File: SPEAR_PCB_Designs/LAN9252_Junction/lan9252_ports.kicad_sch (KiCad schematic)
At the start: 36 parts, among them J1 SM04B-GHS-TB, J2 SM04B-GHS-TB, T1 H1102NLT, T2 H1102NLT, U1 24FC512

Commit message: Almost finished board
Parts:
- removed C1, C2: C, Capacitor_SMD:C_0201_0603Metric, symbol Device:C
- removed C3, C4: 1000 uF, Capacitor_SMD:C_0201_0603Metric, symbol Device:C
- removed J2: SM04B-GHS-TB, Connector_JST:JST_GH_SM04B-GHS-TB_1x04-1MP_P1.25mm_Horizontal, symbol Connector_Generic_MountingPin:Conn_01x04_MountingPin
- removed R1, R2, R3, R4, R5, R6: 49.9 R, Resistor_SMD:R_0603_1608Metric, symbol Device:R_US
- removed T1, T2: H1102NLT, Transformer_SMD:Transformer_Pulse_H1100NL, symbol H1102NLT:H1102NLT
- added C18, C19, C20, C21, C22, C23, C24, C25: 10p, Capacitor_SMD:C_0402_1005Metric, symbol Device:C
- added C26, C27: 22n, Capacitor_SMD:C_0402_1005Metric, symbol Device:C
- added C28, C29: 1000 pF, Capacitor_SMD:C_0402_1005Metric, symbol Device:C
- added J1: SM04B-GHS-TB, Connector_JST:JST_GH_SM04B-GHS-TB_1x04-1MP_P1.25mm_Horizontal, symbol LAN9252 Symbols:SM04B-GHS-TB
- added R10, R11, R12: 49.9R 1%, Resistor_SMD:R_0402_1005Metric, symbol Device:R_US
- added R17: 1k, Resistor_SMD:R_0402_1005Metric, symbol Device:R_US
- added R18, R19: 75R 1%, Resistor_SMD:R_0402_1005Metric, symbol Device:R_US
- added T1, T2: H1102NLT, SPEAR_FOOTPRINTS:XFMR_H1102NLT, symbol LAN9252 Symbols:H1102NLT
- C30: renamed from C5; footprint Capacitor_SMD:C_0201_0603Metric -> Capacitor_SMD:C_0402_1005Metric
- D1, D2, D3: footprint LED_SMD:LED_0201_0603Metric -> LED_SMD:LED_0603_1608Metric
- J2: renamed from J1; symbol Connector_Generic_MountingPin:Conn_01x04_MountingPin -> LAN9252 Symbols:SM04B-GHS-TB; now in the parts list
- R13: value 1k -> 49.9R 1%; footprint Resistor_SMD:R_0603_1608Metric -> Resistor_SMD:R_0402_1005Metric
- R14: value 75 -> 49.9R 1%; footprint Resistor_SMD:R_0603_1608Metric -> Resistor_SMD:R_0402_1005Metric
- R15: value 75 -> 0R; footprint Resistor_SMD:R_0603_1608Metric -> Resistor_SMD:R_0402_1005Metric
- R16: renamed from R10; value 49.9 R -> 0R; footprint Resistor_SMD:R_0603_1608Metric -> Resistor_SMD:R_0402_1005Metric
- R20: renamed from R11; value 75 -> 75R 1%; footprint Resistor_SMD:R_0603_1608Metric -> Resistor_SMD:R_0402_1005Metric
- R21: renamed from R12; value 75 -> 75R 1%; footprint Resistor_SMD:R_0603_1608Metric -> Resistor_SMD:R_0402_1005Metric
- R22: renamed from R16; footprint Resistor_SMD:R_0603_1608Metric -> Resistor_SMD:R_0402_1005Metric
- R23: renamed from R17; footprint Resistor_SMD:R_0603_1608Metric -> Resistor_SMD:R_0402_1005Metric
- R24: renamed from R18; footprint Resistor_SMD:R_0603_1608Metric -> Resistor_SMD:R_0402_1005Metric
- R25: renamed from R19; footprint Resistor_SMD:R_0603_1608Metric -> Resistor_SMD:R_0402_1005Metric
- R26: renamed from R20; footprint Resistor_SMD:R_0603_1608Metric -> Resistor_SMD:R_0402_1005Metric
- R27: renamed from R21; footprint Resistor_SMD:R_0603_1608Metric -> Resistor_SMD:R_0402_1005Metric
- R28: renamed from R22; footprint Resistor_SMD:R_0603_1608Metric -> Resistor_SMD:R_0402_1005Metric
- R29: renamed from R23; footprint Resistor_SMD:R_0603_1608Metric -> Resistor_SMD:R_0402_1005Metric
- R7, R8, R9: value 49.9 R -> 49.9R 1%; footprint Resistor_SMD:R_0603_1608Metric -> Resistor_SMD:R_0402_1005Metric
- renumbered U1 to U2
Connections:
- net GNDREF is gone; now on net GND: C30.2, R23.1, U2.4 (VSS)
- net GND: now also D1.1 (K), C18.2, C19.2, C20.2, C21.2, C22.2, C23.2, C24.2, C25.2, C26.2, C27.2, C28.2, C29.2; no longer D1.2 (A)
- net GPIO1: now also R17.1; no longer R13.1
- net RXA N: now also R13.2, C24.1, T2.3; no longer R7.2
- net RXA P: now also C22.1, R11.2, T2.1
- net RXB N: now also R14.2, C25.1, T1.6; no longer R8.2
- net RXB P: now also C23.1, R12.2, T1.8
- net TXA N: now also R9.2, C20.1, T2.8
- net TXA P: now also R7.2, C18.1, T2.6
- net TXB N: now also C21.1, R10.2, T1.1
- net TXB P: now also R8.2, C19.1, T1.3
- net VDD33TXRX1: now also R13.1, R15.1, R11.1
- net VDD33TXRX2: now also R14.1, R10.1, R12.1
- net at R15.2: now also C26.1, T2.2, T2.7; no longer R14.2
- net at R21.1: now also T2.10
- net at R20.2, R21.2: now also C29.1
- net at R16.2: now also C27.1, T1.2, T1.7
- net TXA+: now reaches J2.1 (Pin_1)
- net TXA+: now also T2.9
- net TXA-: now reaches J2.2 (Pin_2)
- net TXA-: now also T2.11
- net RXA+: now reaches J2.3 (Pin_3)
- net RXA+: now also T2.14
- net RXA-: now reaches J2.4 (Pin_4)
- net RXA-: now also T2.16
- net at R20.1: now also T2.15
- new net: D1.2 (A), R17.2
- new net: R19.1, T1.10
- new net: R18.1, T1.15
- new net: C28.1, R18.2, R19.2
- new net RXB+: J1.3 (Pin_3), T1.14
- new net RXB-: J1.4 (Pin_4), T1.16
- new net TXB+: J1.1 (Pin_1), T1.9
- new net TXB-: J1.2 (Pin_2), T1.11
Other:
- note added: "Polarity, and transmit and receive were swapped for routing purposes. Auto-MDIX and polarity detection will correct for this."
- moved on the sheet: D1, D3, J2, R16, R20, R21, R22, R24, R25, R26, R27

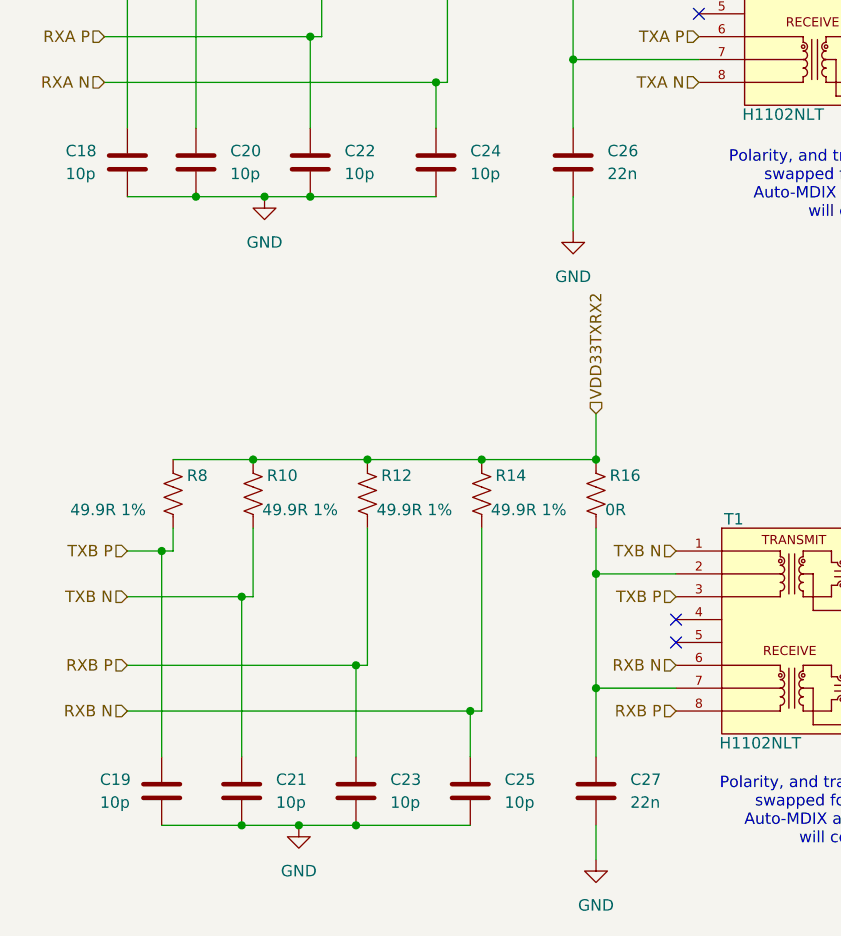
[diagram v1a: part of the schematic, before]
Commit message: Added Fabrication Spec
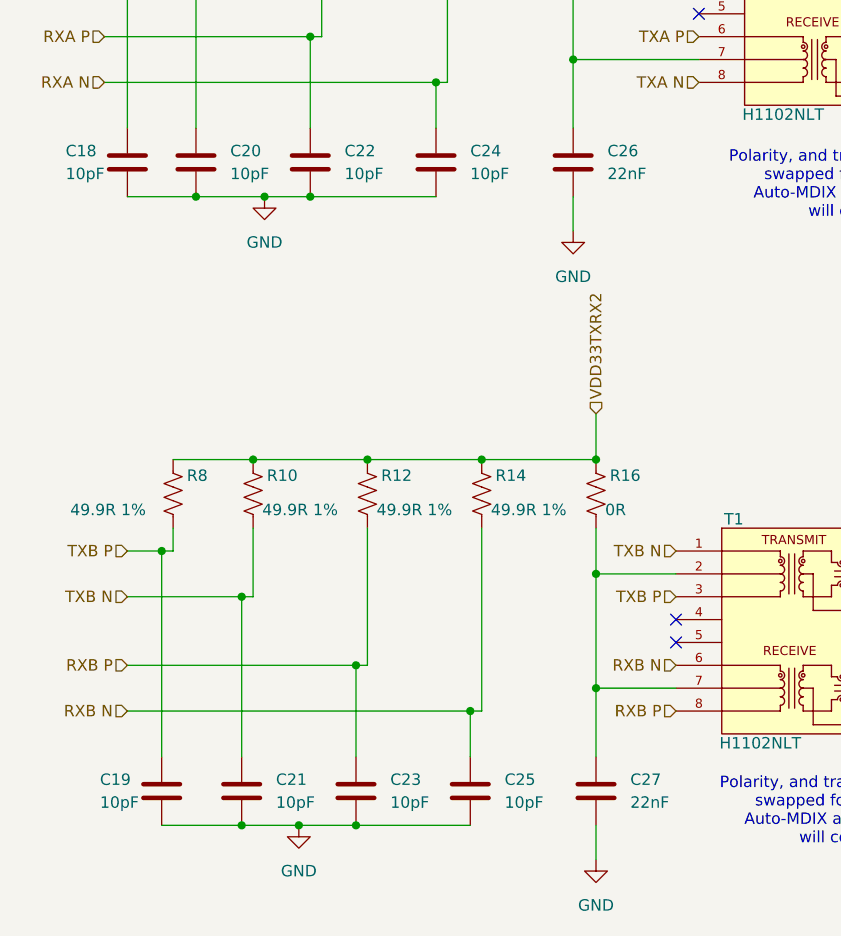
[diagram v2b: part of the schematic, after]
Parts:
- C18, C19, C20, C21, C22, C23, C24, C25: value 10p -> 10pF; DigiKey_Part_Number (none) -> 1276-1139-1-ND
- C26, C27: value 22n -> 22nF; DigiKey_Part_Number (none) -> 399-C0402C223K5RACTUCT-ND
- C28, C29: DigiKey_Part_Number (none) -> 399-C0402C102K5RACTUCT-ND
- C30: DigiKey_Part_Number (none) -> 445-5932-1-ND
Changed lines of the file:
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@@
+			)
+		)
+		(property "DigiKey_Part_Number" "445-5932-1-ND"
+			(at 200.66 125.73 0)
+			(effects
+				(font
+					(size 1.27 1.27)
+				)
+				(hide yes)
 			)
 		)
@@
 		)
 		(property "STANDARD" ""
+			(at 137.16 142.24 0)
+			(effects
+				(font
+					(size 1.27 1.27)
+				)
+				(hide yes)
+			)
+		)
+		(property "DigiKey_Part_Number" "399-C0402C102K5RACTUCT-ND"
 			(at 137.16 142.24 0)
 			(effects
@@
 			)
 		)
-		(property "Value" "10p"
+		(property "Value" "10pF"
 			(at 64.77 77.4699 0)
 			(effects
@@
 		)
 		(property "STANDARD" ""
+			(at 60.96 76.2 0)
+			(effects
+				(font
+					(size 1.27 1.27)
+				)
+				(hide yes)
+			)
+		)
+		(property "DigiKey_Part_Number" "1276-1139-1-ND"
 			(at 60.96 76.2 0)
 			(effects
@@
 			)
 		)
-		(property "Value" "22n"
+		(property "Value" "22nF"
 			(at 82.55 147.3199 0)
 			(effects
@@
 		)
 		(property "STANDARD" ""
+			(at 78.74 146.05 0)
+			(effects
+				(font
+					(size 1.27 1.27)
+				)
+				(hide yes)
+			)
+		)
+		(property "DigiKey_Part_Number" "399-C0402C223K5RACTUCT-ND"
 			(at 78.74 146.05 0)
 			(effects
@@
 			)
 		)
-		(property "Value" "10p"
+		(property "Value" "10pF"
 			(at 43.18 147.3199 0)
 			(effects
@@
 			)
 		)
+		(property "DigiKey_Part_Number" "1276-1139-1-ND"
+			(at 39.37 146.05 0)
+			(effects
+				(font
+					(size 1.27 1.27)
+				)
+				(hide yes)
+			)
+		)
 		(pin "2"
 		)
@@
 			)
 		)
-		(property "Value" "10p"
+		(property "Value" "10pF"
 			(at 23.622 147.32 0)
 			(effects
@@
 		)
 		(property "STANDARD" ""
+			(at 30.48 146.05 0)
+			(effects
+				(font
+					(size 1.27 1.27)
+				)
+				(hide yes)
+			)
+		)
+		(property "DigiKey_Part_Number" "1276-1139-1-ND"
 			(at 30.48 146.05 0)
 			(effects
@@
 			)
 		)
-		(property "Value" "10p"
+		(property "Value" "10pF"
 			(at 68.58 147.3199 0)
 			(effects
@@
 		)
 		(property "STANDARD" ""
+			(at 64.77 146.05 0)
+			(effects
+				(font
+					(size 1.27 1.27)
+				)
+				(hide yes)
+			)
+		)
+		(property "DigiKey_Part_Number" "1276-1139-1-ND"
 			(at 64.77 146.05 0)
 			(effects
@@
 			)
 		)
-		(property "Value" "10p"
+		(property "Value" "10pF"
 			(at 55.88 147.3199 0)
 			(effects
@@
 		)
 		(property "STANDARD" ""
+			(at 52.07 146.05 0)
+			(effects
+				(font
+					(size 1.27 1.27)
+				)
+				(hide yes)
+			)
+		)
+		(property "DigiKey_Part_Number" "1276-1139-1-ND"
 			(at 52.07 146.05 0)
 			(effects
@@
 			)
 		)
-		(property "Value" "10p"
+		(property "Value" "10pF"
 			(at 38.1 77.4699 0)
 			(effects
@@
 		)
 		(property "STANDARD" ""
+			(at 34.29 76.2 0)
+			(effects
+				(font
+					(size 1.27 1.27)
+				)
+				(hide yes)
+			)
+		)
+		(property "DigiKey_Part_Number" "1276-1139-1-ND"
 			(at 34.29 76.2 0)
 			(effects
@@
 			)
 		)
-		(property "Value" "10p"
+		(property "Value" "10pF"
 			(at 50.8 77.4699 0)
 			(effects
@@
 			)
 		)
+		(property "DigiKey_Part_Number" "1276-1139-1-ND"
+			(at 46.99 76.2 0)
+			(effects
+				(font
+					(size 1.27 1.27)
+				)
+				(hide yes)
+			)
+		)
 		(pin "2"
 		)
@@
 			)
 		)
-		(property "Value" "22n"
+		(property "Value" "22nF"
 			(at 80.01 77.4699 0)
 			(effects
@@
 			)
 		)
+		(property "DigiKey_Part_Number" "399-C0402C223K5RACTUCT-ND"
+			(at 76.2 76.2 0)
+			(effects
+				(font
+					(size 1.27 1.27)
+				)
+				(hide yes)
+			)
+		)
 		(pin "2"
 		)
@@
 			)
 		)
-		(property "Value" "10p"
+		(property "Value" "10pF"
 			(at 19.812 77.47 0)
 			(effects
@@
 			)
 		)
+		(property "DigiKey_Part_Number" "1276-1139-1-ND"
+			(at 26.67 76.2 0)
+			(effects
+				(font
+					(size 1.27 1.27)
+				)
+				(hide yes)
+			)
+		)
 		(pin "2"
 		)
@@
 			(at 147.32 72.39 0)
 			(effects
+				(font
+					(size 1.27 1.27)
+				)
+				(hide yes)
+			)
+		)
+		(property "DigiKey_Part_Number" "399-C0402C102K5RACTUCT-ND"
+			(at 147.32 72.39 0)
+			(effects

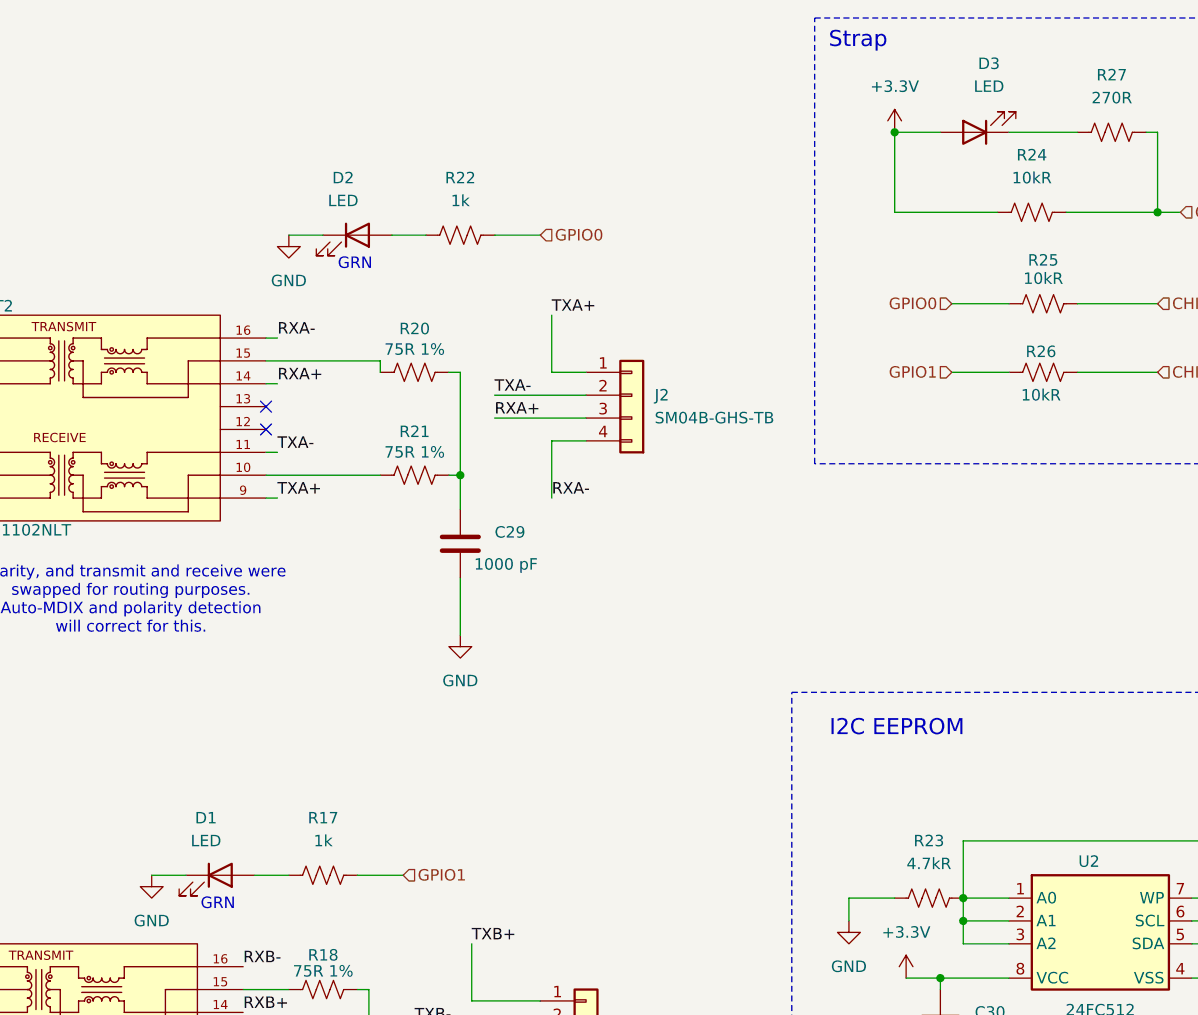
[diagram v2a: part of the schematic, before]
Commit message: Added BOM for the Junction Board
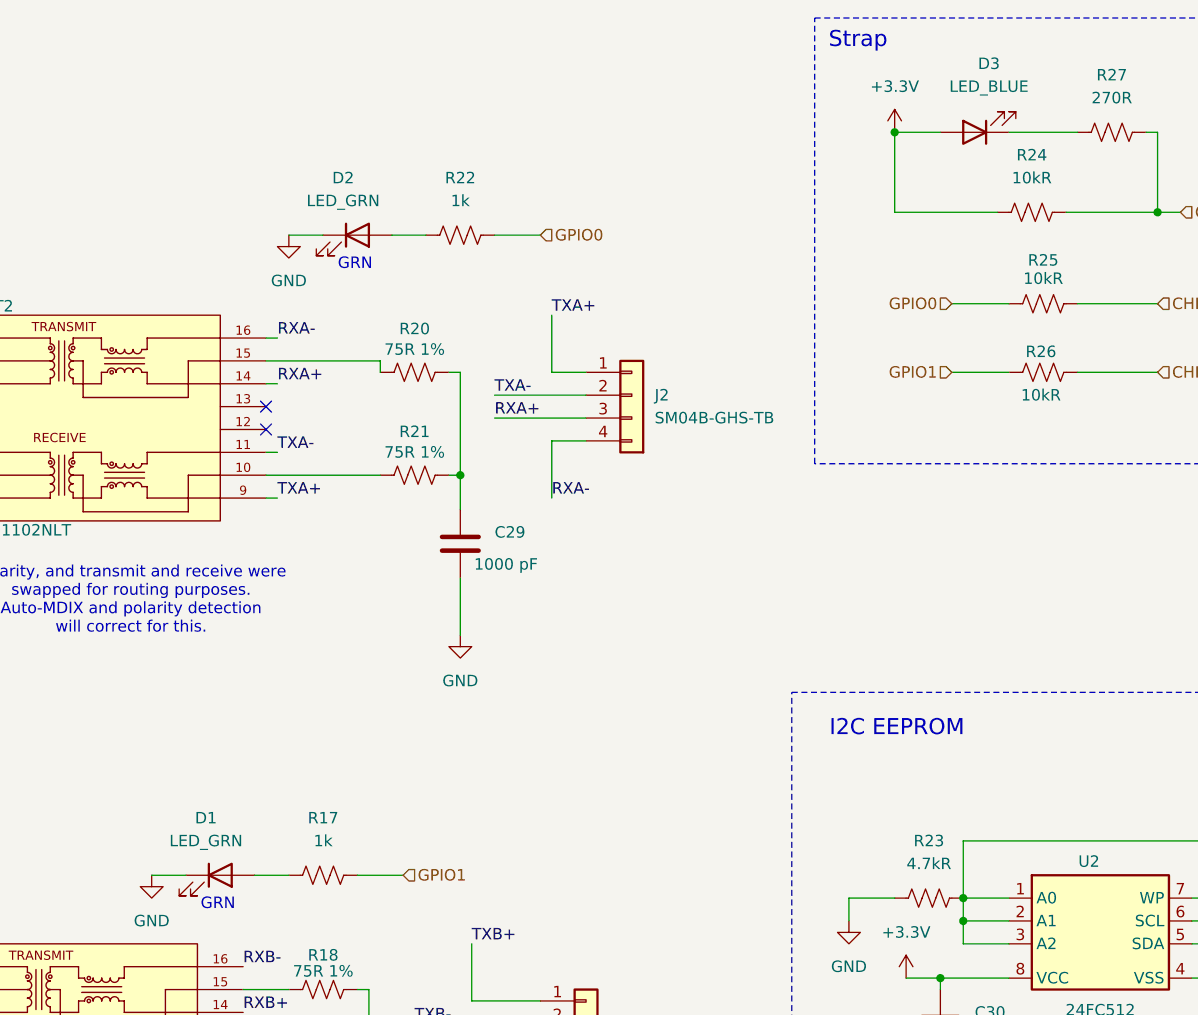
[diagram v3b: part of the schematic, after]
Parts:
- D1, D2: value LED -> LED_GRN; DigiKey_Part_Number (none) -> 732-12017-1-ND
- D3: value LED -> LED_BLUE; DigiKey_Part_Number (none) -> 732-12013-1-ND
- J1, J2: DigiKey_Part_Number (none) -> 455-1566-1-ND
- R10, R11, R12, R13, R14, R7, R8, R9: DigiKey_Part_Number (none) -> 311-49.9LRCT-ND
- R15, R16: DigiKey_Part_Number (none) -> 311-0.0JRCT-ND
- R17, R22: DigiKey_Part_Number (none) -> 311-1.0KJRCT-ND
- R18, R19, R20, R21: DigiKey_Part_Number (none) -> 13-RC0402FR-1375RLCT-ND
- R23: DigiKey_Part_Number (none) -> 311-4.7KJRCT-ND
- R24, R25, R26: DigiKey_Part_Number (none) -> 311-10KJRCT-ND
- R27: DigiKey_Part_Number (none) -> 311-270LRCT-ND
- R28, R29: DigiKey_Part_Number (none) -> YAG2303CT-ND
- T1, T2: DigiKey_Part_Number (none) -> 553-1532-1-ND
- U2: DigiKey_Part_Number (none) -> 24FC512-I/SN-ND
